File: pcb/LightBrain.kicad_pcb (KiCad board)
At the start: 2 copper layers, 36.8 x 46.4 mm, 60 parts, among them J1 Wago2060, J2 Wago2060, J3 Wago2060, J5 Wago2060, Q1 AO3401A, SW1 SW_Push, SW2 SW_Push, SW3 SW_Push, U1 SN75176BDR, U10 TP6841S6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

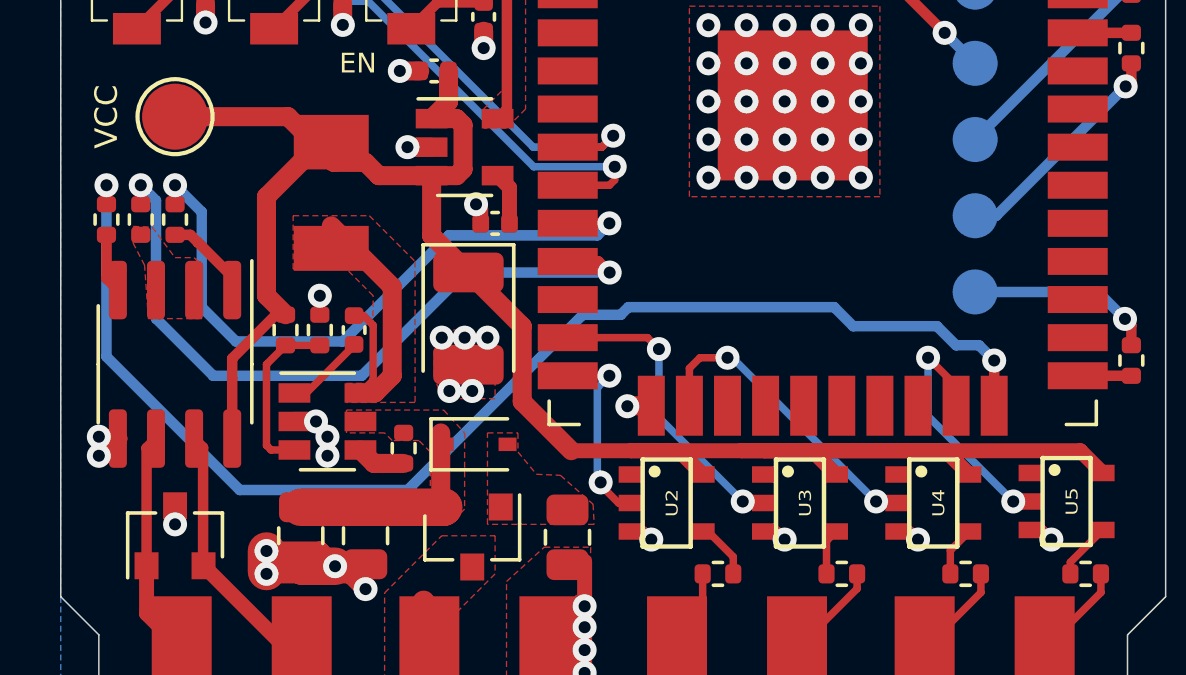
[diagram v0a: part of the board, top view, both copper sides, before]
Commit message: More examples: vvvv, micropython; fix in gerbers; added firmware binary
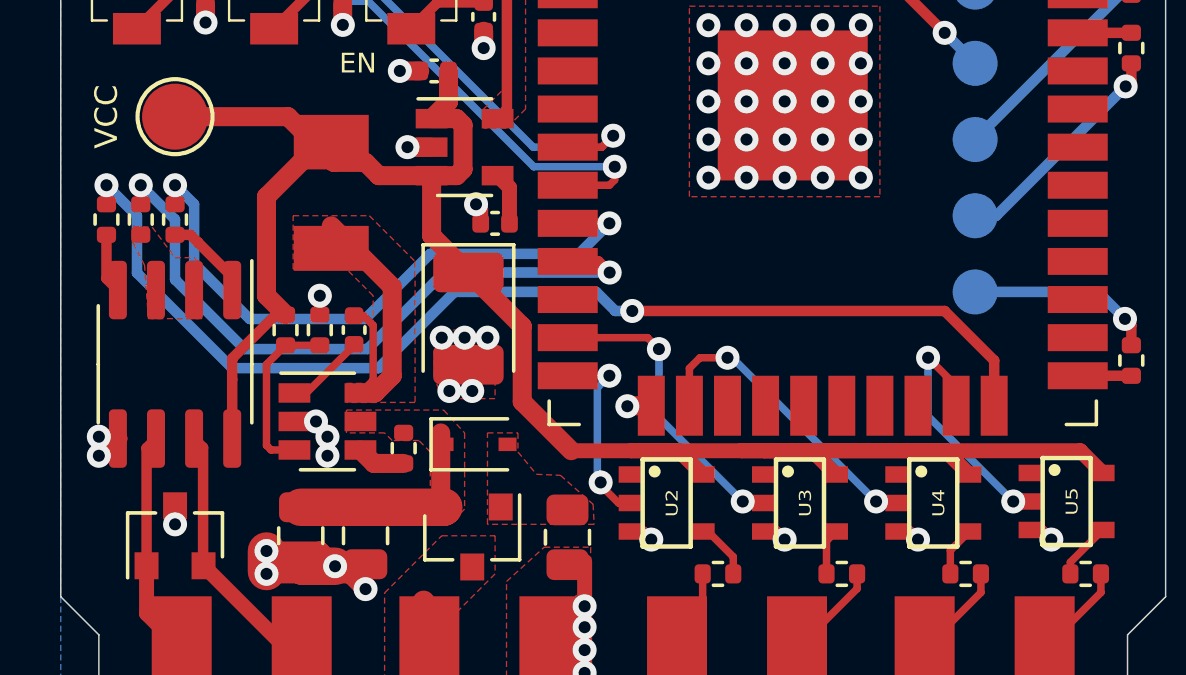
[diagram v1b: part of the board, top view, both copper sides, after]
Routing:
- net /485_TX: track 42.5 -> 37.4 mm
- net /485_RT: track 24.2 -> 22.3 mm
- net /485_RX: track 22.1 -> 20.8 mm
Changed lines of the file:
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@@
   (segment (start 216.025 92.964) (end 216.027 92.966) (width 0.35) (layer "F.Cu") (net 21))
   (segment (start 214.24 92.964) (end 216.025 92.964) (width 0.35) (layer "F.Cu") (net 21))
+  (segment (start 211.455 92.456) (end 209.804 90.805) (width 0.35) (layer "F.Cu") (net 22))
   (segment (start 181.864 86.614) (end 181.864 87.247) (width 0.35) (layer "F.Cu") (net 22))
+  (segment (start 209.804 90.805) (end 199.39 90.805) (width 0.35) (layer "F.Cu") (net 22))
   (segment (start 211.455 93.964) (end 211.455 92.456) (width 0.35) (layer "F.Cu") (net 22))
-  (via (at 211.455 92.456) (size 0.8) (drill 0.4) (layers "F.Cu" "B.Cu") (net 22))
+  (via (at 199.39 90.805) (size 0.8) (drill 0.4) (layers "F.Cu" "B.Cu") (net 22))
   (via (at 181.864 86.614) (size 0.8) (drill 0.4) (layers "F.Cu" "B.Cu") (net 22))
-  (segment (start 206.756 91.313) (end 206.121 90.678) (width 0.35) (layer "B.Cu") (net 22))
-  (segment (start 199.009 90.932) (end 197.743002 90.932) (width 0.35) (layer "B.Cu") (net 22))
-  (segment (start 191.901002 96.774) (end 186.309 96.774) (width 0.35) (layer "B.Cu") (net 22))
-  (segment (start 211.455 92.456) (end 210.947 91.948) (width 0.35) (layer "B.Cu") (net 22))
-  (segment (start 206.121 90.678) (end 199.263 90.678) (width 0.35) (layer "B.Cu") (net 22))
-  (segment (start 197.743002 90.932) (end 191.901002 96.774) (width 0.35) (layer "B.Cu") (net 22))
-  (segment (start 181.864 92.329) (end 181.864 86.614) (width 0.35) (layer "B.Cu") (net 22))
-  (segment (start 186.309 96.774) (end 181.864 92.329) (width 0.35) (layer "B.Cu") (net 22))
-  (segment (start 210.185 91.948) (end 209.55 91.313) (width 0.35) (layer "B.Cu") (net 22))
-  (segment (start 209.55 91.313) (end 206.756 91.313) (width 0.35) (layer "B.Cu") (net 22))
-  (segment (start 210.947 91.948) (end 210.185 91.948) (width 0.35) (layer "B.Cu") (net 22))
-  (segment (start 199.263 90.678) (end 199.009 90.932) (width 0.35) (layer "B.Cu") (net 22))
+  (segment (start 182.88 89.535) (end 182.88 87.63) (width 0.35) (layer "B.Cu") (net 22))
+  (segment (start 198.187617 90.17) (end 193.468675 90.17) (width 0.35) (layer "B.Cu") (net 22))
+  (segment (start 186.055 92.71) (end 182.88 89.535) (width 0.35) (layer "B.Cu") (net 22))
+  (segment (start 199.39 90.805) (end 198.822617 90.805) (width 0.35) (layer "B.Cu") (net 22))
+  (segment (start 182.88 87.63) (end 181.864 86.614) (width 0.35) (layer "B.Cu") (net 22))
+  (segment (start 190.928675 92.71) (end 186.055 92.71) (width 0.35) (layer "B.Cu") (net 22))
+  (segment (start 193.468675 90.17) (end 190.928675 92.71) (width 0.35) (layer "B.Cu") (net 22))
+  (segment (start 198.822617 90.805) (end 198.187617 90.17) (width 0.35) (layer "B.Cu") (net 22))
   (segment (start 210.185 93.298031) (end 209.250965 92.363996) (width 0.25) (layer "F.Cu") (net 23))
   (segment (start 212.668 97.155) (end 212.09 97.155) (width 0.25) (layer "F.Cu") (net 23))
@@
   (via (at 183.007 86.614) (size 0.8) (drill 0.4) (layers "F.Cu" "B.Cu") (net 34))
   (via (at 198.637356 89.524414) (size 0.8) (drill 0.4) (layers "F.Cu" "B.Cu") (net 34))
-  (segment (start 193.812586 89.524414) (end 198.637356 89.524414) (width 0.35) (layer "B.Cu") (net 34))
-  (segment (start 183.515 87.122) (end 183.515 91.059) (width 0.35) (layer "B.Cu") (net 34))
-  (segment (start 185.42 92.964) (end 190.373 92.964) (width 0.35) (layer "B.Cu") (net 34))
-  (segment (start 183.007 86.614) (end 183.515 87.122) (width 0.35) (layer "B.Cu") (net 34))
-  (segment (start 190.373 92.964) (end 193.812586 89.524414) (width 0.35) (layer "B.Cu") (net 34))
-  (segment (start 183.515 91.059) (end 185.42 92.964) (width 0.35) (layer "B.Cu") (net 34))
+  (segment (start 186.46775 92.075) (end 190.5635 92.075) (width 0.35) (layer "B.Cu") (net 34))
+  (segment (start 184.15 89.75725) (end 186.46775 92.075) (width 0.35) (layer "B.Cu") (net 34))
+  (segment (start 183.007 86.614) (end 184.15 87.757) (width 0.35) (layer "B.Cu") (net 34))
+  (segment (start 184.15 87.757) (end 184.15 89.75725) (width 0.35) (layer "B.Cu") (net 34))
+  (segment (start 190.5635 92.075) (end 193.114086 89.524414) (width 0.35) (layer "B.Cu") (net 34))
+  (segment (start 193.114086 89.524414) (end 198.637356 89.524414) (width 0.35) (layer "B.Cu") (net 34))
   (segment (start 197.24 87.884) (end 198.628 87.884) (width 0.35) (layer "F.Cu") (net 35))
   (segment (start 184.15 87.247) (end 184.15 86.614) (width 0.25) (layer "F.Cu") (net 35))
   (via (at 198.628 87.884) (size 0.8) (drill 0.4) (layers "F.Cu" "B.Cu") (net 35))
   (via (at 184.15 86.614) (size 0.8) (drill 0.4) (layers "F.Cu" "B.Cu") (net 35))
-  (segment (start 185.039 87.503) (end 184.15 86.614) (width 0.35) (layer "B.Cu") (net 35))
-  (segment (start 198.228001 88.283999) (end 193.275001 88.283999) (width 0.35) (layer "B.Cu") (net 35))
-  (segment (start 198.628 87.884) (end 198.228001 88.283999) (width 0.35) (layer "B.Cu") (net 35))
-  (segment (start 185.039 90.678) (end 185.039 87.503) (width 0.35) (layer "B.Cu") (net 35))
-  (segment (start 189.738 91.821) (end 186.182 91.821) (width 0.35) (layer "B.Cu") (net 35))
-  (segment (start 193.275001 88.283999) (end 189.738 91.821) (width 0.35) (layer "B.Cu") (net 35))
-  (segment (start 186.182 91.821) (end 185.039 90.678) (width 0.35) (layer "B.Cu") (net 35))
+  (segment (start 186.639005 91.071505) (end 184.785 89.2175) (width 0.35) (layer "B.Cu") (net 35))
+  (segment (start 198.628 87.884) (end 197.612 88.9) (width 0.35) (layer "B.Cu") (net 35))
+  (segment (start 197.612 88.9) (end 192.659 88.9) (width 0.35) (layer "B.Cu") (net 35))
+  (segment (start 192.659 88.9) (end 190.487495 91.071505) (width 0.35) (layer "B.Cu") (net 35))
+  (segment (start 184.785 87.249) (end 184.15 86.614) (width 0.35) (layer "B.Cu") (net 35))
+  (segment (start 190.487495 91.071505) (end 186.639005 91.071505) (width 0.35) (layer "B.Cu") (net 35))
+  (segment (start 184.785 89.2175) (end 184.785 87.249) (width 0.35) (layer "B.Cu") (net 35))
   (segment (start 194.437 80.5206) (end 192.9002 80.5206) (width 0.35) (layer "F.Cu") (net 38))
   (segment (start 194.437 79.5294) (end 194.437 80.5206) (width 0.35) (layer "F.Cu") (net 38))
